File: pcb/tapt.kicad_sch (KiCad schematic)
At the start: 38 parts, among them J1 Conn_01x05_Pin, J2 Conn_01x04_MountingPin, SW1 SW_SPDT_LIMIT, SW2 SW_SPST, U1 nRF52810-QCxx, Y1 32MHz, Y2 32.768kHz

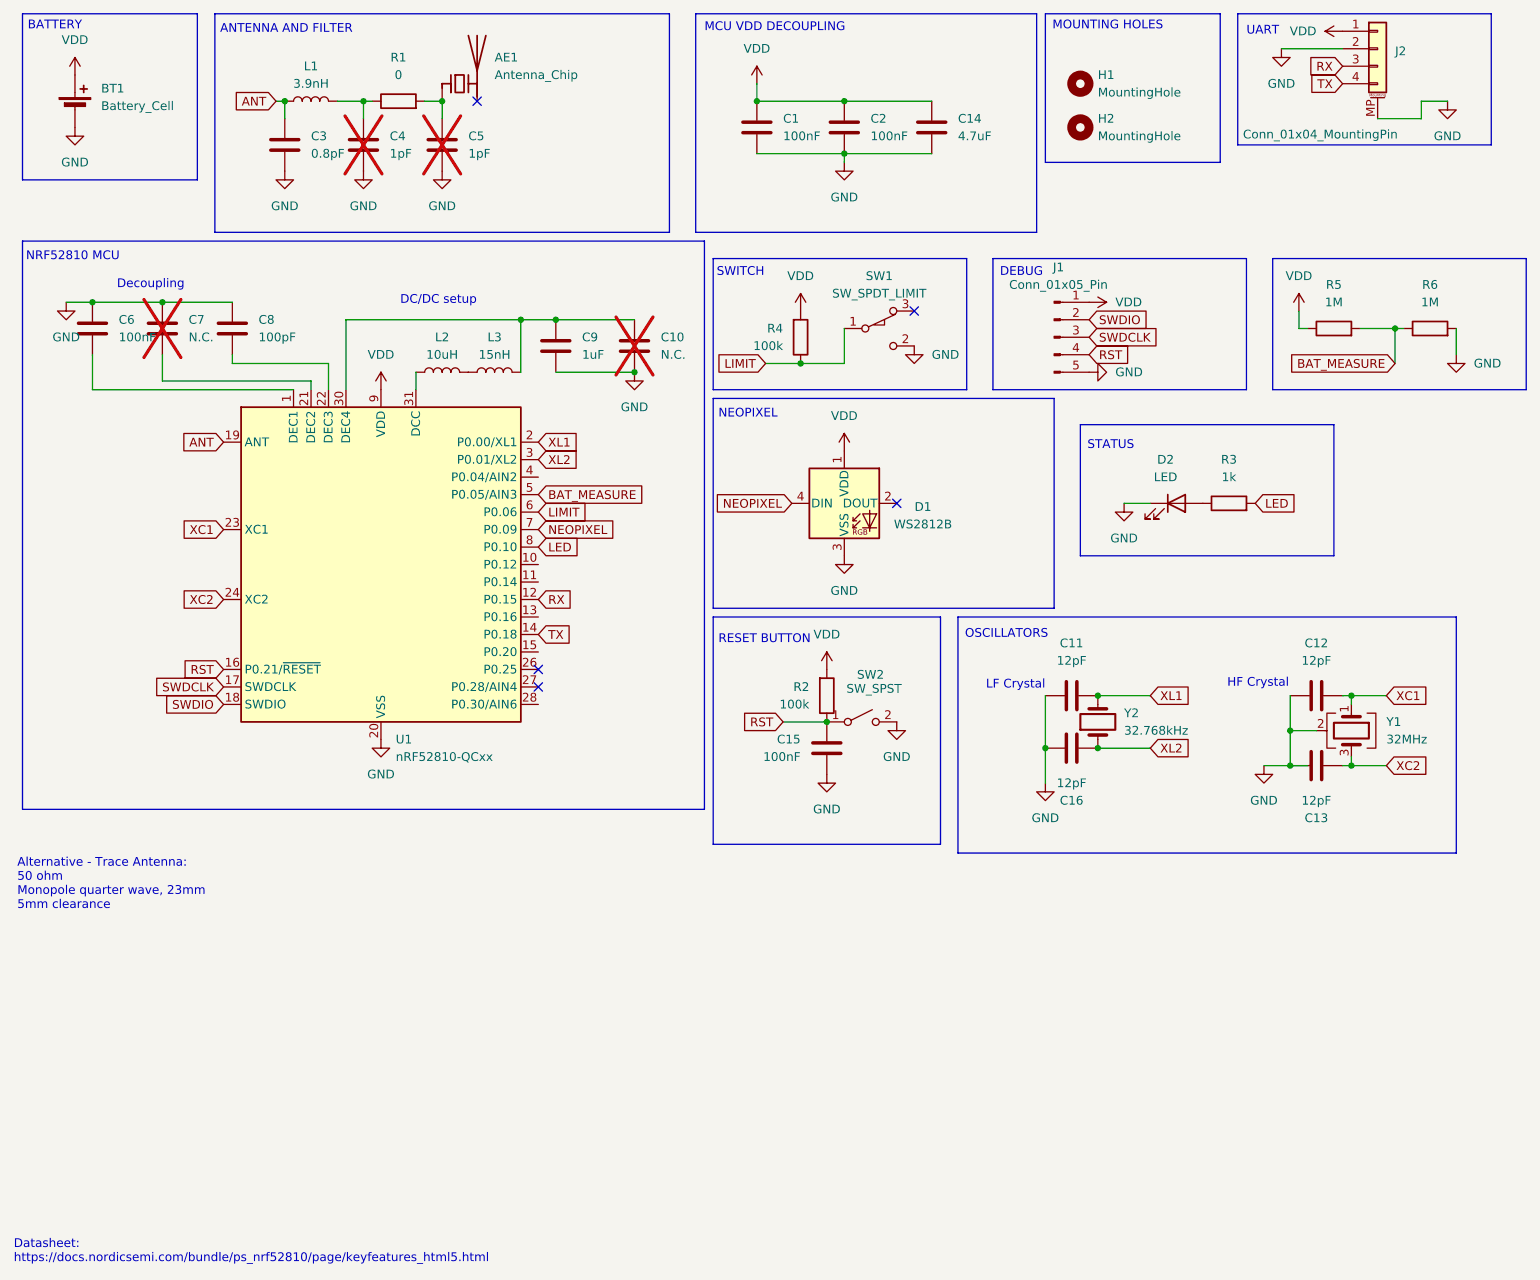
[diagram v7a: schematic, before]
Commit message: pcb: voltage divider, antenna t-network
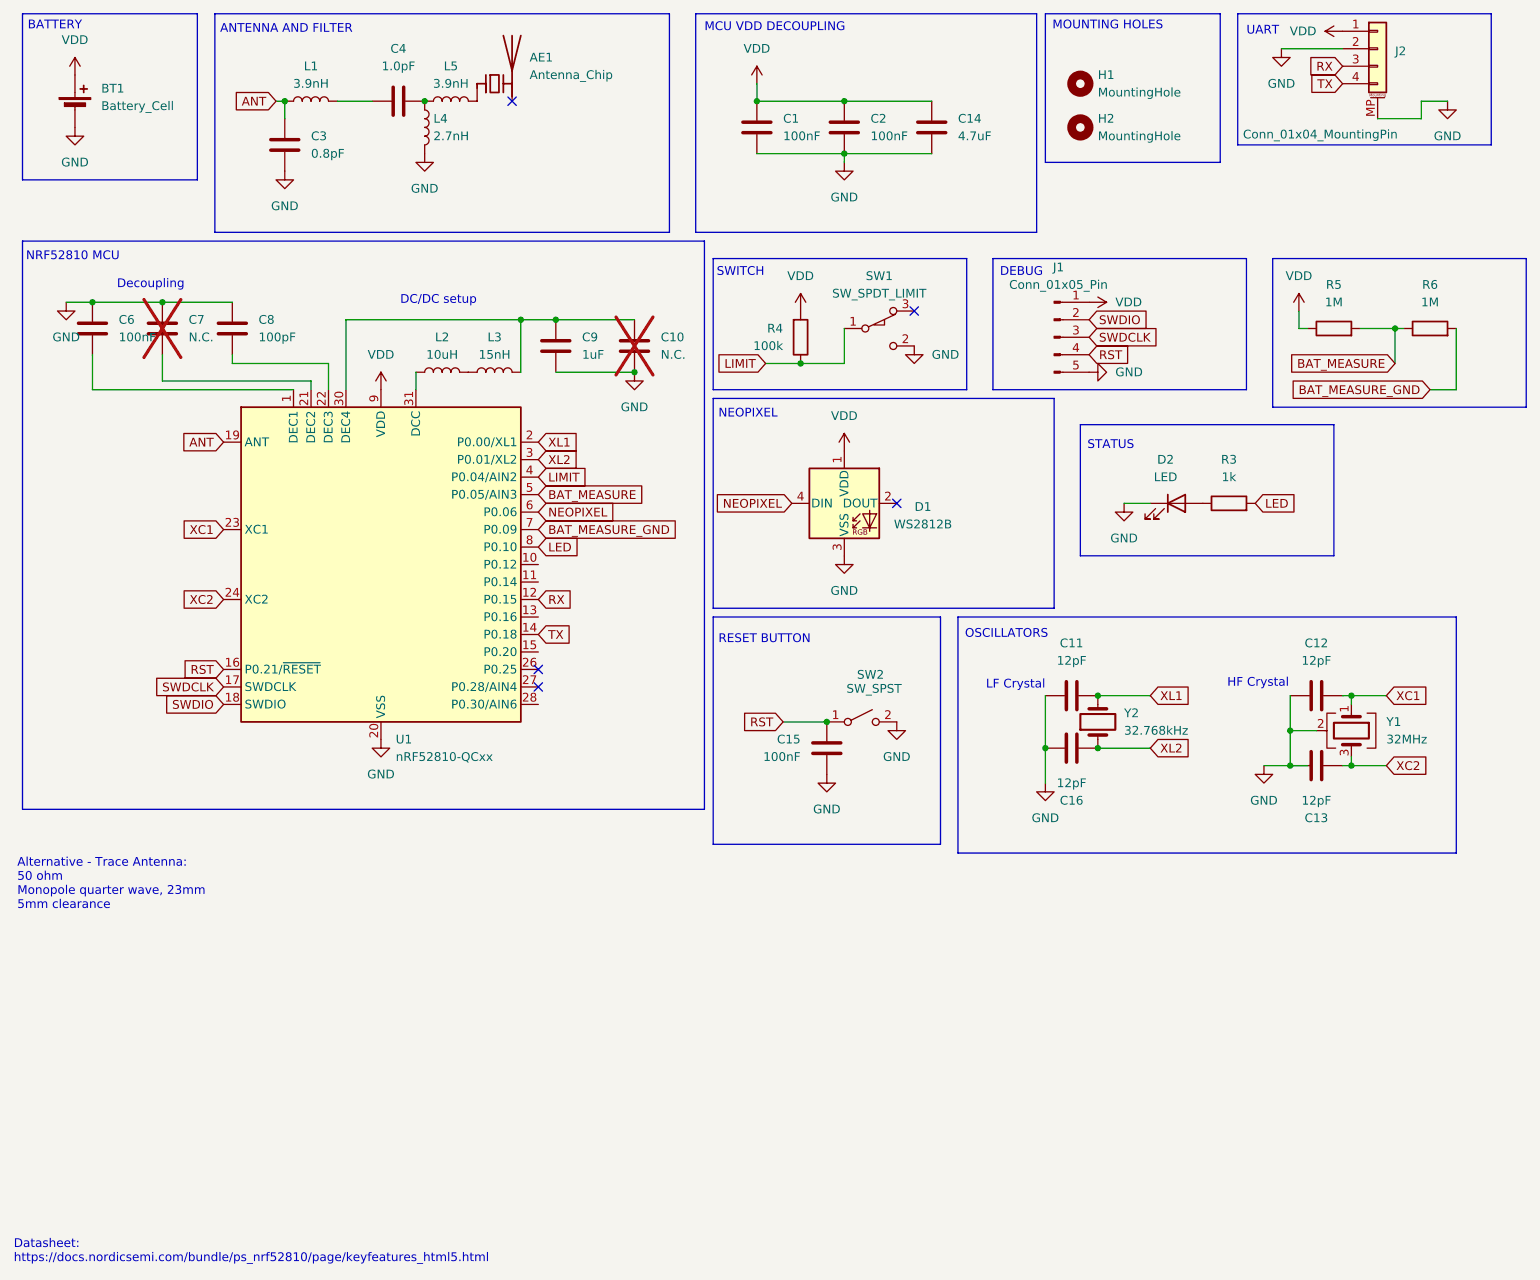
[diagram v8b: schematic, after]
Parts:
- removed C5: 1pF, Capacitor_SMD:C_0402_1005Metric, symbol Device:C
- removed R1: 0, Resistor_SMD:R_0402_1005Metric, symbol Device:R
- removed R2: 100k, Resistor_SMD:R_0402_1005Metric, symbol Device:R
- added L4: 2.7nH, Inductor_SMD:L_0402_1005Metric, symbol Device:L
- added L5: 3.9nH, Inductor_SMD:L_0402_1005Metric, symbol Device:L
- C4: value 1pF -> 1.0pF; LCSC (none) -> C1550; now fitted
- H1, H2: footprint MountingHole:MountingHole_2.7mm_M2.5 -> MountingHole:MountingHole_3.2mm_M3
- J1: now left out of the parts list
- L1: footprint Capacitor_SMD:C_0402_1005Metric -> Inductor_SMD:L_0402_1005Metric
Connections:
- net GND: now also L4.2; no longer C4.2, R6.2
- net LIMIT: now also U1.4 (P0.04/AIN2); no longer U1.6 (P0.06)
- net NEOPIXEL: now also U1.6 (P0.06); no longer U1.7 (P0.09)
- net at AE1.1 (FEED): now also L5.2
- new net: C4.2, L4.1, L5.1
- new net BAT_MEASURE_GND: R6.2, U1.7 (P0.09)
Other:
- moved on the sheet: AE1
